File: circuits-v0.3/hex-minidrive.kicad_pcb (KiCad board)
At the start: 4 copper layers, 29 x 51 mm, 97 parts, among them X1 16MHz

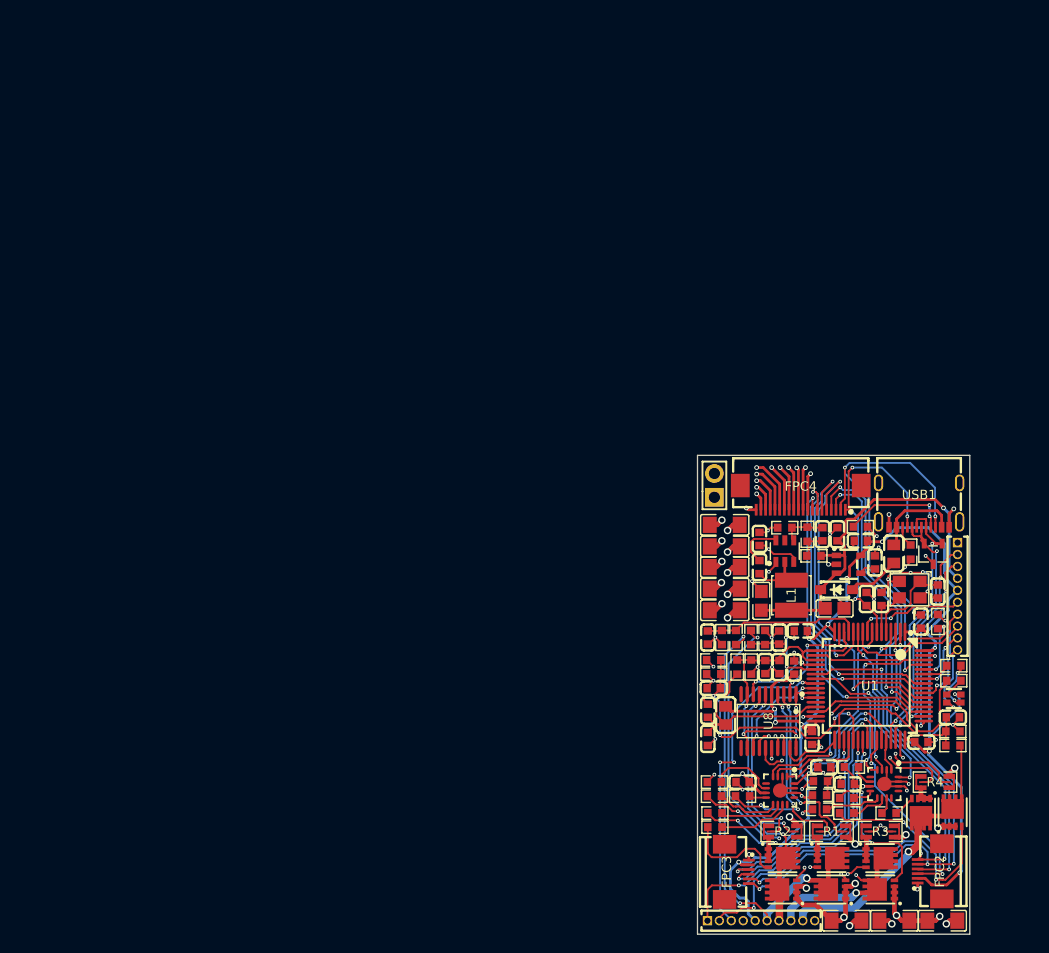
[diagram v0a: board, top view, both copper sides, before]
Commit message: Sketch out v0.3 of the servo driver, without the USB port.
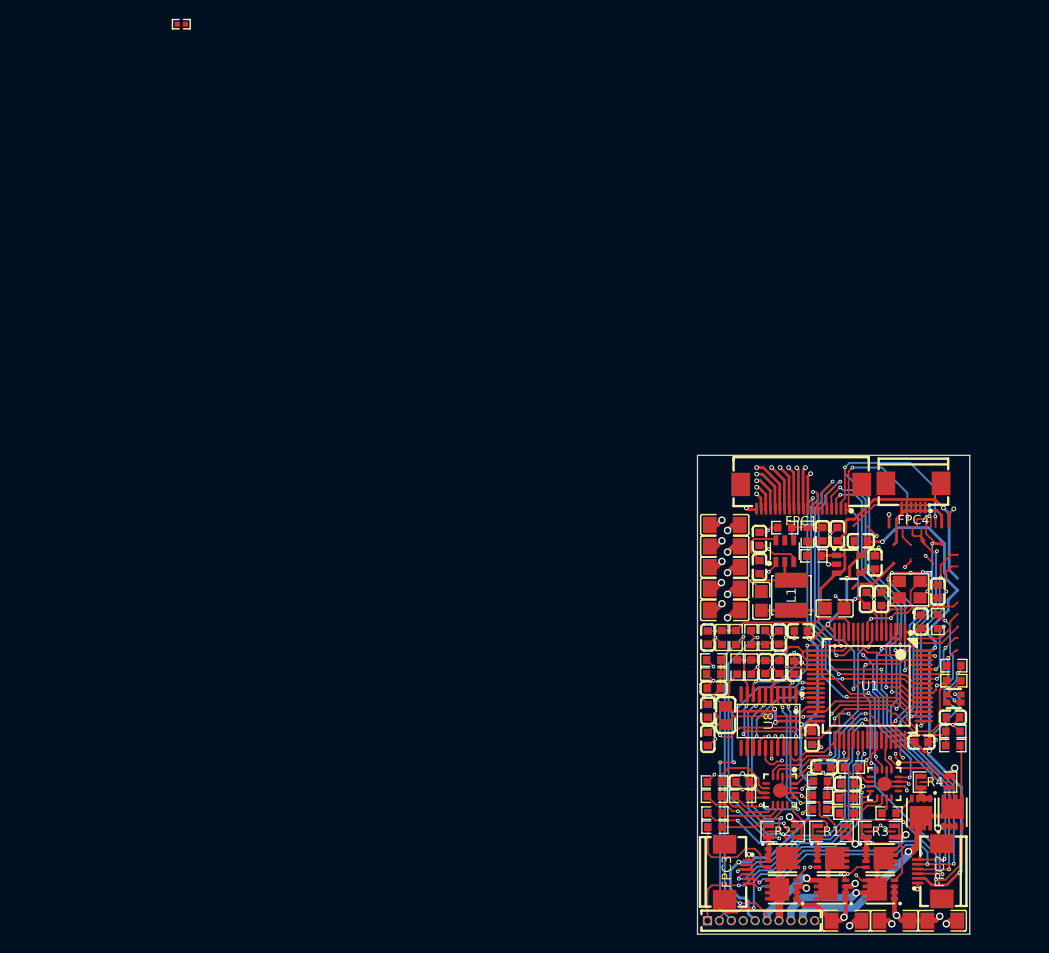
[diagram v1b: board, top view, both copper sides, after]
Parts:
- removed D1: ~, Library:SOD-123_L2.7-W1.6-LS3.7-RD-1
- removed D2: ~, Library:SOT-23-3_L3.0-W1.7-P0.95-LS2.9-BR
- removed H2: 2P-2.54mm-header, Library:HDR-TH_2P-P2.54-V-M
- removed H3: 10P 1.27mm header, Library:HDR-TH_HX-PZ1.27-1X10P-ZZ
- removed L3: 300mΩ, Library:L0805
- removed R11, R12: 5.1kΩ, Library:R0603
- removed USB1: ~, Library:USB-C-SMD_TYPE-C16PIN
- added FPC1: ~, Library:FPC-SMD_20P-P0.50_XUNPU_FPC-05F-20PH20, F.Cu at (67.0, 50.9)
- added R7: 20kΩ, Library:R0402, F.Cu at (1.02, 0.57)
- FPC4: footprint Library:FPC-SMD_20P-P0.50_XUNPU_FPC-05F-20PH20 -> Library:FPC-SMD_6P-P0.50_XUNPU_FPC-05F-6PH20
- moved FPC4 12.0 mm to (79.0, 50.8)
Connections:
- FPC4 pad 1: NRST -> GND
- FPC4 pad 2: BOOT0/STOP -> SYS_JTCK-SWCLK
- FPC4 pad 3: USART3_RX -> SYS_JTMS-SVDIO
- FPC4 pad 4: USART3_TX -> 5V
- FPC4 pad 5: SPI3_MOSI -> 3V3
- FPC4 pad 6: SPI3_MISO -> BOOT0/STOP
- FPC4 pad 7: SPI3_SCK -> unconnected-(FPC4-Pad7)
- FPC4 pad 8: SPI3_NSS -> unconnected-(FPC4-Pad8)
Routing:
- net (no net): track 0.00 -> 28.8 mm, vias 0 -> 2
- net Net-(USB1-CC1): track 11.5 -> 0.00 mm, vias 2 -> 0
- net USB:5V: track 9.52 -> 0.00 mm
- net Net-(D1-+): track 5.55 -> 0.00 mm
- net Net-(USB1-CC2): track 2.29 -> 0.00 mm

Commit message: Think about v0.3 driver circuit.
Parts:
- removed C101, C201, C301, C401: 1nF, Library:C0603
- removed FPC4: ~, Library:FPC-SMD_6P-P0.50_XUNPU_FPC-05F-6PH20
- removed R7: 20kΩ, Library:R0402
- moved C7 81.8 mm to (-6.95, 29.7)
- moved C8 81.8 mm to (-4.45, 30.4)
- moved C9 81.8 mm to (-2.95, 32.7)
- moved R10 81.8 mm to (-9.45, 32.0)
- moved R5 81.8 mm to (-10.2, 29.7)
- moved C1 81.8 mm to (-15.2, 33.2)
- moved C2 81.8 mm to (-15.2, 30.2)
- moved C4 81.8 mm to (-15.1, 36.8)
- moved C5 81.8 mm to (-7.25, 37.6)
- moved C6 81.8 mm to (-8.55, 29.7)
- moved L1 81.8 mm to (-11.8, 36.2)
- moved R6 81.8 mm to (-12.6, 29.0)
- moved U3 81.8 mm to (-5.75, 32.9)
- moved U4 81.8 mm to (-12.6, 31.5)
- moved C3 79.1 mm to (-13.7, 26.9)
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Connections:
- FPC2 pad 5: FREE_IO_1 -> SYS_JTCK-SWCLK
- FPC2 pad 6: FREE_IO_2 -> SYS_JTMS-SVDIO
- FPC3 pad 5: FREE_IO_1 -> SYS_JTCK-SWCLK
- FPC3 pad 6: FREE_IO_2 -> SYS_JTMS-SVDIO
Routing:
- net 3V3: track 143.5 -> 0.00 mm, vias 13 -> 0
- net GND: track 123.3 -> 0.00 mm, vias 64 -> 0
- net VCC: track 68.4 -> 0.00 mm, vias 22 -> 0
- net FREE_IO_1: track 54.5 -> 0.00 mm, vias 4 -> 0
- net FREE_IO_2: track 52.9 -> 0.00 mm, vias 4 -> 0
- net M1: track 48.0 -> 0.00 mm, vias 3 -> 0
- net BOOT0/STOP: track 46.3 -> 0.00 mm, vias 3 -> 0
- net ADC1_IN3/HALF_3V3_REF: track 40.7 -> 0.00 mm, vias 4 -> 0
- net 5V: track 40.5 -> 0.00 mm, vias 1 -> 0
- net SPI3_MOSI: track 37.2 -> 0.00 mm, vias 2 -> 0
- net M2: track 36.7 -> 0.00 mm, vias 2 -> 0
- net SPI3_MISO: track 35.3 -> 0.00 mm, vias 2 -> 0
- net I2C2_SCL: track 34.9 -> 0.00 mm, vias 2 -> 0
- net TIM3_CH3/ENCODER_3: track 34.5 -> 0.00 mm, vias 3 -> 0
- net SPI3_SCK: track 33.8 -> 0.00 mm, vias 2 -> 0
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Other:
- board size 29 x 51 mm -> 34.9 x 50 mm

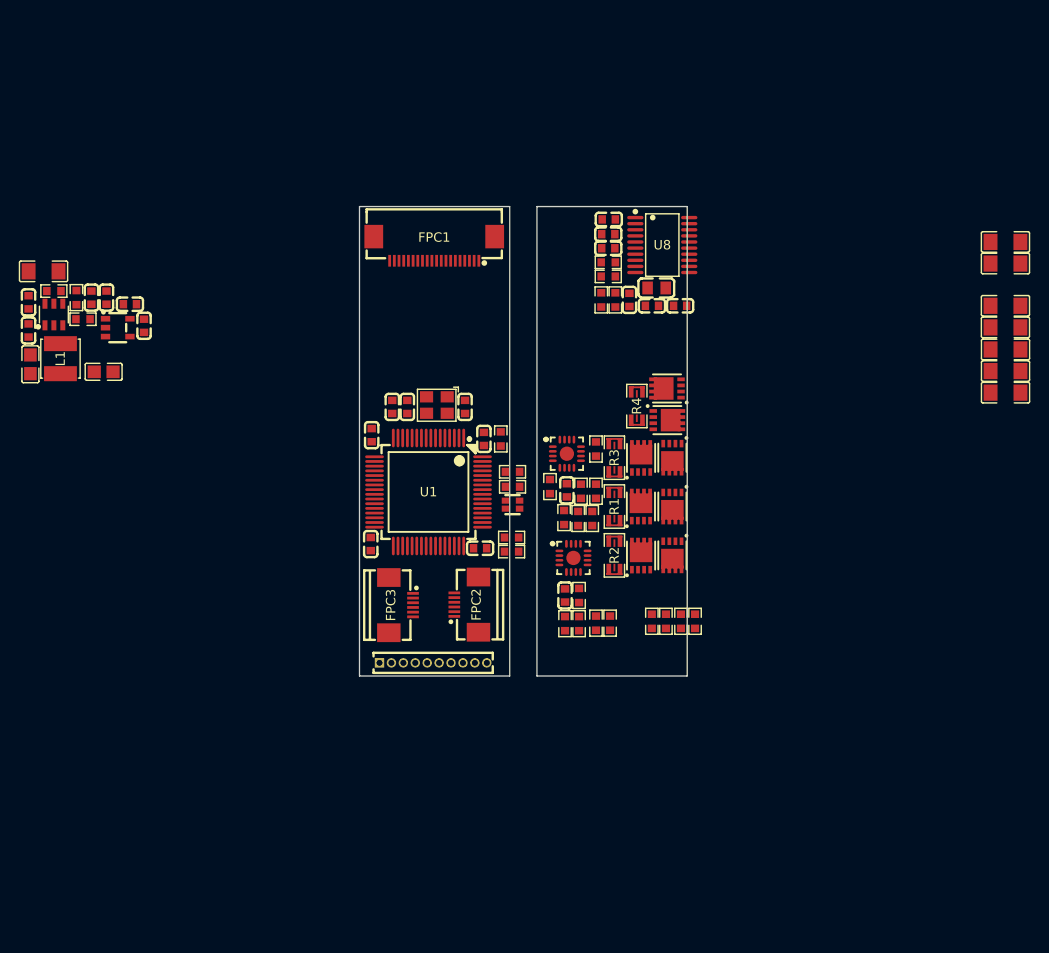
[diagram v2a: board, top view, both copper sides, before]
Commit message: Start re-wiring v0.3 motor driver, 16mm width is too tight.
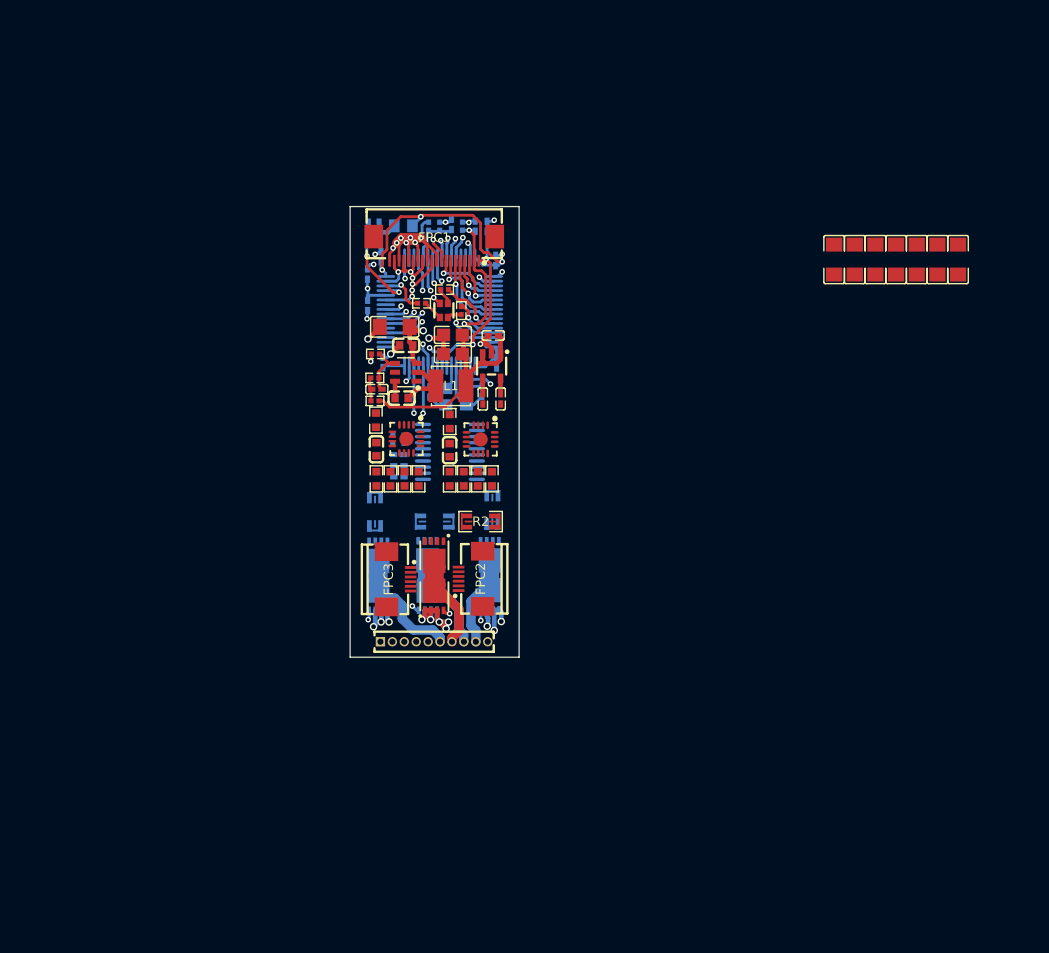
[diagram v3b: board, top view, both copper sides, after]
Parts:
- removed C10, C11, C14, C15, C16, C17, C18: 10uF, Library:C1206
- removed C12, C7, C8, C803: 1uF, Library:C0603
- removed C13, C24, C25, C26, C27, C801, C802: 100nF, Library:C0603
- removed C20: 15pF, Library:C0603
- removed C30: 1nF, Library:C0603
- removed C34, C9: 10nF, Library:C0603
- removed R10: 49.9Ω, Library:R0603
- removed R103, R203, R303, R403, R5: 100kΩ, Library:R0603
- removed R104, R204, R304, R404: 5.1kΩ, Library:R0603
- removed R21, R22, R23: 1.5kΩ, Library:R0603
- removed R6: 13kΩ, Library:R0603
- removed R801, R802: 10kΩ, Library:R0603
- removed U8: ~, Library:TSSOP-20_L6.5-W4.4-P0.65-LS6.4-BL
- added C0: 10uF, Library:C1206, F.Cu at (70.5, 25.6)
- added C101: 100nF, Library:C0402, B.Cu at (22.1, 22.2)
- added C102: 1uF, Library:C0402, B.Cu at (20.9, 22.2)
- added C103: 15pF, Library:C0402, B.Cu at (33.0, 39.7)
- added C104: 15pF, Library:C0402, B.Cu at (27.5, 39.7)
- added C105: 1uF, Library:C0402, B.Cu at (20.9, 27.2)
- added C106: 100nF, Library:C0402, B.Cu at (20.9, 30.5)
- added C107: 1uF, Library:C0402, B.Cu at (24.2, 46.4)
- added C108: 100nF, Library:C0402, B.Cu at (24.2, 47.6)
- added C109: 100nF, Library:C0402, B.Cu at (34.5, 25.8)
- added C110: 100nF, Library:C0402, B.Cu at (33.6, 22.1)
- added C111: 100nF, Library:C0402, B.Cu at (34.6, 36.6)
- added C112: 100nF, Library:C0402, B.Cu at (22.5, 36.6)
- added C113: 100nF, Library:C0402, B.Cu at (22.3, 25.4)
- added C114: 100nF, Library:C0402, B.Cu at (32.3, 22.1)
- added C115: 1nF, Library:C0402, B.Cu at (29.8, 21.9)
- added C31: 1uF, Library:C0402, F.Cu at (34.2, 33.7)
- added C32: 1uF, Library:C0402, F.Cu at (35.0, 40.5)
- added C33: 10nF, Library:C0402, F.Cu at (33.1, 40.5)
- added C41: 10uF, Library:C1206, F.Cu at (23.8, 32.8)
- added C42: 100nF, Library:C0603, F.Cu at (25.0, 34.8)
- added C43: 100nF, Library:C0603, F.Cu at (24.5, 40.4)
- added C44: 22uF, Library:C0805, F.Cu at (29.9, 33.7)
- added C45: 22uF, Library:C0805, F.Cu at (29.9, 35.7)
- added C46: 100pF, Library:C0402, F.Cu at (21.9, 39.5)
- added R11: 10kΩ, Library:R0402, B.Cu at (31.0, 22.1)
- added R12: 10kΩ, Library:R0402, B.Cu at (24.8, 44.8)
- added R13: 10kΩ, Library:R0402, B.Cu at (23.6, 44.8)
- added R15: 1.5kΩ, Library:R0402, F.Cu at (30.8, 31.1)
- added R16: 1.5kΩ, Library:R0402, F.Cu at (26.6, 30.3)
- added R19: 10kΩ, Library:R0402, B.Cu at (28.5, 22.1)
- added R41: 49.9Ω, Library:R0402, F.Cu at (21.6, 40.7)
- added R42: 100kΩ, Library:R0402, F.Cu at (21.6, 38.2)
- added R43: 13.3kΩ, Library:R0402, F.Cu at (21.7, 35.7)
- added U2: ~, Library:TSSOP-20_L6.5-W4.4-P0.65-LS6.4-BL, B.Cu at (29.6, 46.1)
- C1, C2: value 100nF -> 10uF; footprint Library:C0603 -> Library:C1206
- C21: value 15pF -> 100nF; footprint Library:C0603 -> Library:C0402; moved to B.Cu
- C4, C5: value 22uF -> 10uF; footprint Library:C0805 -> Library:C1206
- C6: value 100pF -> 10uF; footprint Library:C0603 -> Library:C1206
- L2, Q1, Q2, Q5, Q6, Q7, Q8, R1, R3, R4, U1, X1: moved to B.Cu
- R101, R102, R201, R202, R301, R302, R401, R402: value 10Ω -> 4.7Ω
- R17: value 100kΩ -> 1.5kΩ; footprint Library:R0603 -> Library:R0402
- R18: value 10kΩ -> 100kΩ; footprint Library:R0603 -> Library:R0402; moved to B.Cu
- moved C4 95.1 mm to (79.3, 25.6)
- moved C6 92.4 mm to (83.8, 25.6)
- moved C3 90.8 mm to (77.2, 25.6), turned to -90 degrees
- moved C2 90.3 mm to (75.0, 25.6)
- moved C5 89.6 mm to (81.5, 25.6), turned to -90 degrees
- moved C1 88.3 mm to (72.8, 25.6)
- moved L1 41.7 mm to (29.7, 39.1), turned to 0 degrees
- moved U3 40.0 mm to (34.1, 37.0), turned to 0 degrees
- moved U4 38.0 mm to (24.9, 37.6), turned to -90 degrees
- moved Q2 32.7 mm to (22.0, 61.5), turned to 90 degrees
- moved Q6 29.9 mm to (27.3, 61.5), turned to 90 degrees
- moved R501 29.6 mm to (21.8, 42.8)
- moved Q8 29.0 mm to (33.9, 61.4), turned to 90 degrees
- moved Q1 28.5 mm to (22.0, 57.1), turned to -90 degrees
- moved L2 27.8 mm to (24.7, 22.1), turned to 180 degrees
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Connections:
- C1 pad 1: /Buck-Bootstrap-Capacitor -> GND
- C1 pad 2: /Buck-Output-SW -> VCC
- C21 pad 2: /OSC2 -> 3V3
- C4 pad 2: 5V -> VCC
- C5 pad 2: 5V -> VCC
- C6 pad 1: Buck-FB -> GND
- C6 pad 2: /Buck-Probe-Point -> VCC
- FPC2 pad 5: SYS_JTCK-SWCLK -> SYS_JTMS-SVDIO
- FPC2 pad 6: SYS_JTMS-SVDIO -> SYS_JTCK-SWCLK
- FPC3 pad 5: SYS_JTCK-SWCLK -> SYS_JTMS-SVDIO
- FPC3 pad 6: SYS_JTMS-SVDIO -> SYS_JTCK-SWCLK
- R17 pad 1: ADC2_IN15/VOLTAGE -> TIM4_CH1/RED_LED
- R17 pad 2: VCC -> /Red-LED
- R18 pad 1: GND -> ADC2_IN15/VOLTAGE
- R18 pad 2: ADC2_IN15/VOLTAGE -> VCC
- U1 pad 10: ADC1_IN8/POT_2 -> unconnected-(U1-PC2-Pad10)
- U1 pad 13: OPAMP1_VINP/M1_VOLTAGE -> unconnected-(U1-PA1-Pad13)
- U1 pad 14: ADC1_IN3/HALF_3V3_REF -> ADC1_IN3/HALF_VREF
- U1 pad 17: ADC1_IN3/HALF_3V3_REF -> unconnected-(U1-PA3-Pad17)
- U1 pad 18: ADC2_IN17/POT_3 -> unconnected-(U1-PA4-Pad18)
- U1 pad 19: ADC1_IN3/HALF_3V3_REF -> unconnected-(U1-PA5-Pad19)
- U1 pad 21: OPAMP2_VINP/M2_VOLTAGE -> unconnected-(U1-PA7-Pad21)
- U1 pad 26: ADC1_IN3/HALF_3V3_REF -> unconnected-(U1-PB2-Pad26)
- U1 pad 28: unconnected-(U1-VREF+-Pad28) -> VREF
- U1 pad 3: FREE_IO_1 -> unconnected-(U1-PC14-OSC32_IN-Pad3)
- U1 pad 34: ADC1_IN11/M4_VOLTAGE -> unconnected-(U1-PB12-Pad34)
- U1 pad 35: OPAMP3_VINP/M3_VOLTAGE -> unconnected-(U1-PB13-Pad35)
- U1 pad 4: FREE_IO_2 -> unconnected-(U1-PC15-OSC32_OUT-Pad4)
- U1 pad 45: USB_D_N -> unconnected-(U1-PA11-Pad45)
- U1 pad 46: USB_D_P -> unconnected-(U1-PA12-Pad46)
- U1 pad 55: DIRECTION_SWITCH -> unconnected-(U1-PD2-Pad55)
- U1 pad 58: TOOL_SWITCH -> unconnected-(U1-PB5-Pad58)
- U1 pad 9: ADC1_IN7/POT_1 -> unconnected-(U1-PC1-Pad9)
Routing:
- net VCC: track 0.00 -> 51.3 mm, vias 0 -> 19
- net GND: track 0.00 -> 49.4 mm, vias 0 -> 21
- net 3V3: track 0.00 -> 36.6 mm, vias 0 -> 4
- net 5V: track 0.00 -> 25.2 mm
- net NRST: track 0.00 -> 18.4 mm, vias 0 -> 2
- net BOOT0/STOP: track 0.00 -> 17.8 mm, vias 0 -> 2
- net M1: track 0.00 -> 13.6 mm
- net 3V3A: track 0.00 -> 12.9 mm, vias 0 -> 2
- net M3: track 0.00 -> 11.4 mm
- net M2: track 0.00 -> 10.8 mm
- net M4: track 0.00 -> 10.6 mm
- net SPI3_SCK: track 0.00 -> 9.36 mm, vias 0 -> 1
- net SPI3_MISO: track 0.00 -> 8.78 mm, vias 0 -> 1
- net SPI3_NSS: track 0.00 -> 7.49 mm, vias 0 -> 1
- net SPI3_MOSI: track 0.00 -> 7.26 mm, vias 0 -> 1
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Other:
- board size 34.9 x 50 mm -> 18 x 48 mm
- board text removed: "GND VCC"
